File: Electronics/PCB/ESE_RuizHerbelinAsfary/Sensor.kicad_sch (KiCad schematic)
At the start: 0 parts

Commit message: Add files via upload
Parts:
- added J?: Conn_01x04_Female, symbol Connector:Conn_01x04_Female
- added J?: Conn_01x03_Female, symbol Connector:Conn_01x03_Female
- added J? (x4): Conn_01x05_Female, symbol Connector:Conn_01x05_Female
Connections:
- new net +3.3V: J?.1 (Pin_1)
- new net +5V: J?.1 (Pin_1), J?.1 (Pin_1), J?.1 (Pin_1), J?.1 (Pin_1), J?.1 (Pin_1), J?.2 (Pin_2), J?.2 (Pin_2)
- new net AVDD: J?.2 (Pin_2)
- new net GND: J?.2 (Pin_2), J?.2 (Pin_2), J?.3 (Pin_3), J?.4 (Pin_4)
- new net OE1: J?.3 (Pin_3)
- new net OE2: J?.3 (Pin_3)
- new net Out: J?.5 (Pin_5), J?.5 (Pin_5)
- new net S2: J?.3 (Pin_3), J?.3 (Pin_3)
- new net S3: J?.4 (Pin_4), J?.4 (Pin_4)
- new net Vin: J?.2 (Pin_2)
- new net Vout: J?.3 (Pin_3)
- no-connect marks 0 -> 4
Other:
- note added: "Capteur TOF"
- note added: "Capteur couleur 1"
- note added: "Capteur couleur 2"
- note added: "Capteur infra"
- company: (none) -> ENSEA
- title: (none) -> ESE Project Sensor block

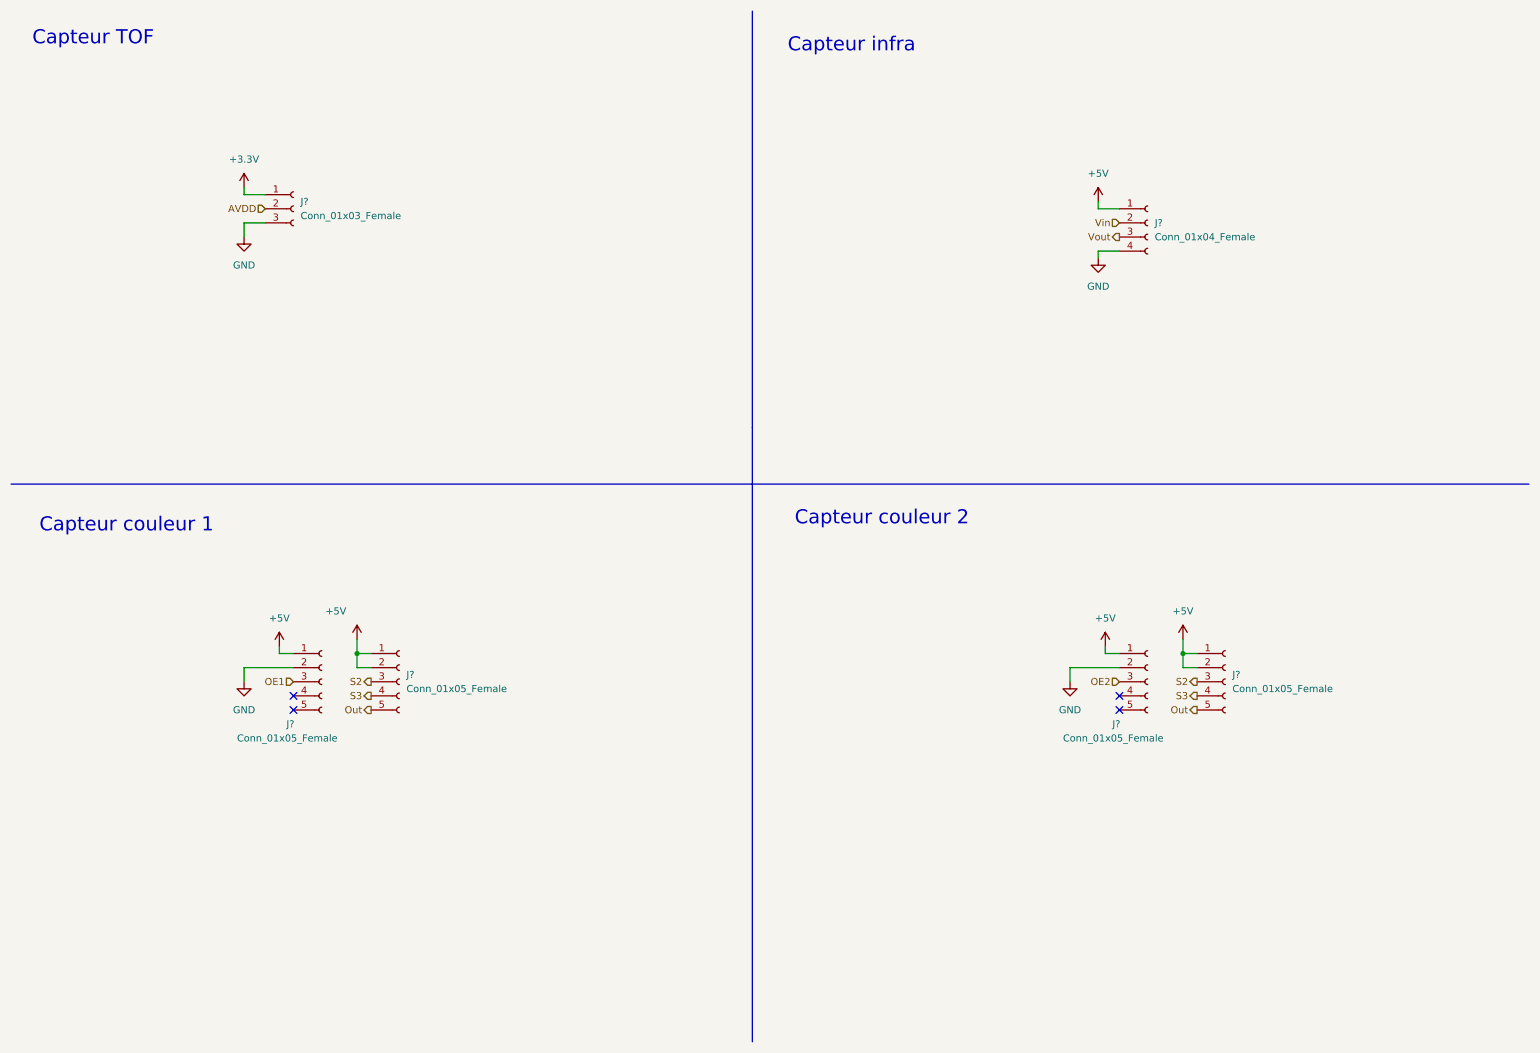
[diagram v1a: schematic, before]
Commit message: added test pin
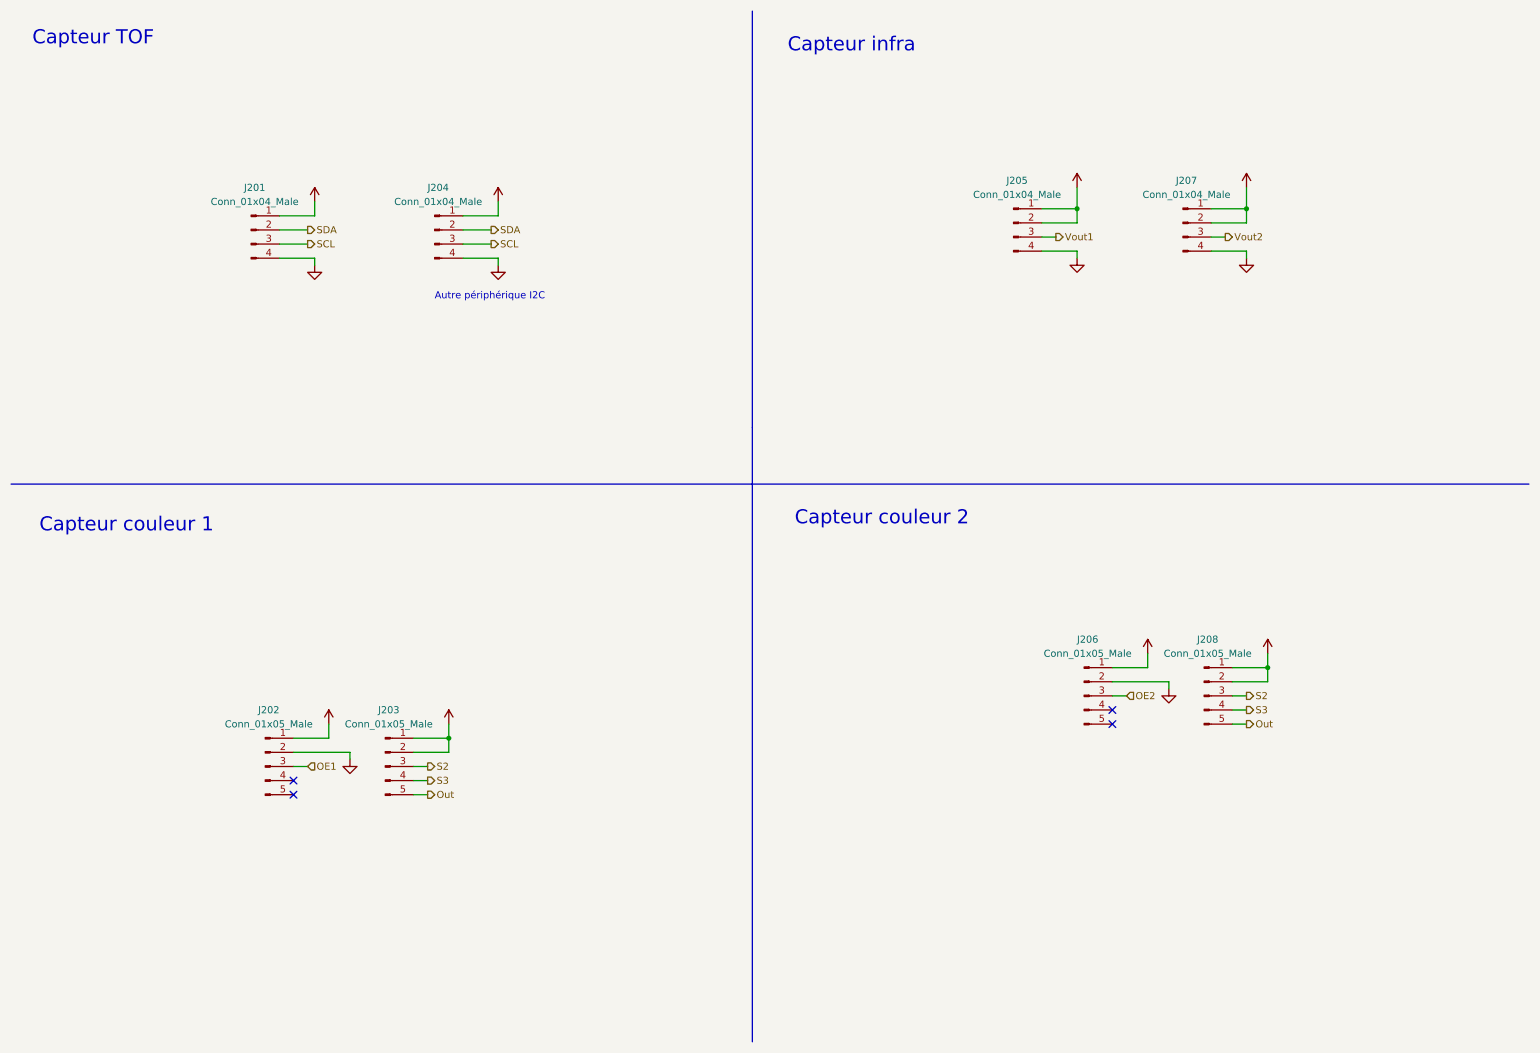
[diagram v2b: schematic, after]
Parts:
- removed J?: Conn_01x04_Female, symbol Connector:Conn_01x04_Female
- removed J?: Conn_01x03_Female, symbol Connector:Conn_01x03_Female
- removed J? (x4): Conn_01x05_Female, symbol Connector:Conn_01x05_Female
- added J201, J204, J205, J207: Conn_01x04_Male, symbol Connector:Conn_01x04_Male
- added J202, J203, J206, J208: Conn_01x05_Male, symbol Connector:Conn_01x05_Male
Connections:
- net +3.3V: now also J201.1 (Pin_1), J204.1 (Pin_1)
- net +5V: now also J202.1 (Pin_1), J203.1 (Pin_1), J203.2 (Pin_2), J205.1 (Pin_1), J205.2 (Pin_2), J206.1 (Pin_1), J207.1 (Pin_1), J207.2 (Pin_2), J208.1 (Pin_1), J208.2 (Pin_2)
- net GND: now also J201.4 (Pin_4), J202.2 (Pin_2), J204.4 (Pin_4), J205.4 (Pin_4), J206.2 (Pin_2), J207.4 (Pin_4)
- net OE1: now also J202.3 (Pin_3)
- net OE2: now also J206.3 (Pin_3)
- net Out: now also J203.5 (Pin_5), J208.5 (Pin_5)
- net S2: now also J203.3 (Pin_3), J208.3 (Pin_3)
- net S3: now also J203.4 (Pin_4), J208.4 (Pin_4)
- new net SCL: J201.3 (Pin_3), J204.3 (Pin_3)
- new net SDA: J201.2 (Pin_2), J204.2 (Pin_2)
- new net Vout1: J205.3 (Pin_3)
- new net Vout2: J207.3 (Pin_3)
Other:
- note added: "Autre périphérique I2C"
